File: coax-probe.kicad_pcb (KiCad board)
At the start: 2 copper layers, 28 x 41 mm, 33 parts, among them J1 Conn_01x02, J2 SMA, J3 Conn_01x02, J4 Conn_01x03, J5 SMA, J6 Conn_01x02, U1 OPA690, U2 INA128, U3 OPA690, U4 CJ431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

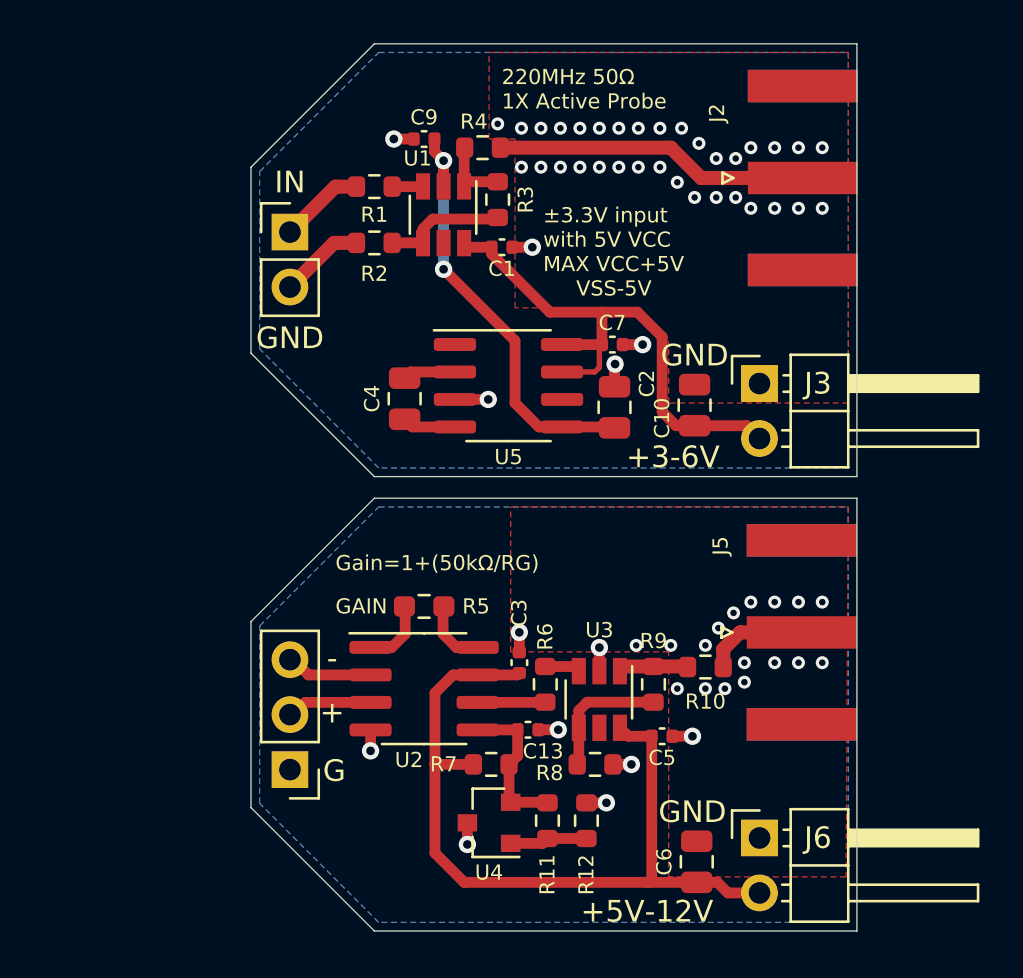
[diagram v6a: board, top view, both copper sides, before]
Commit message: Try out the LMH6642
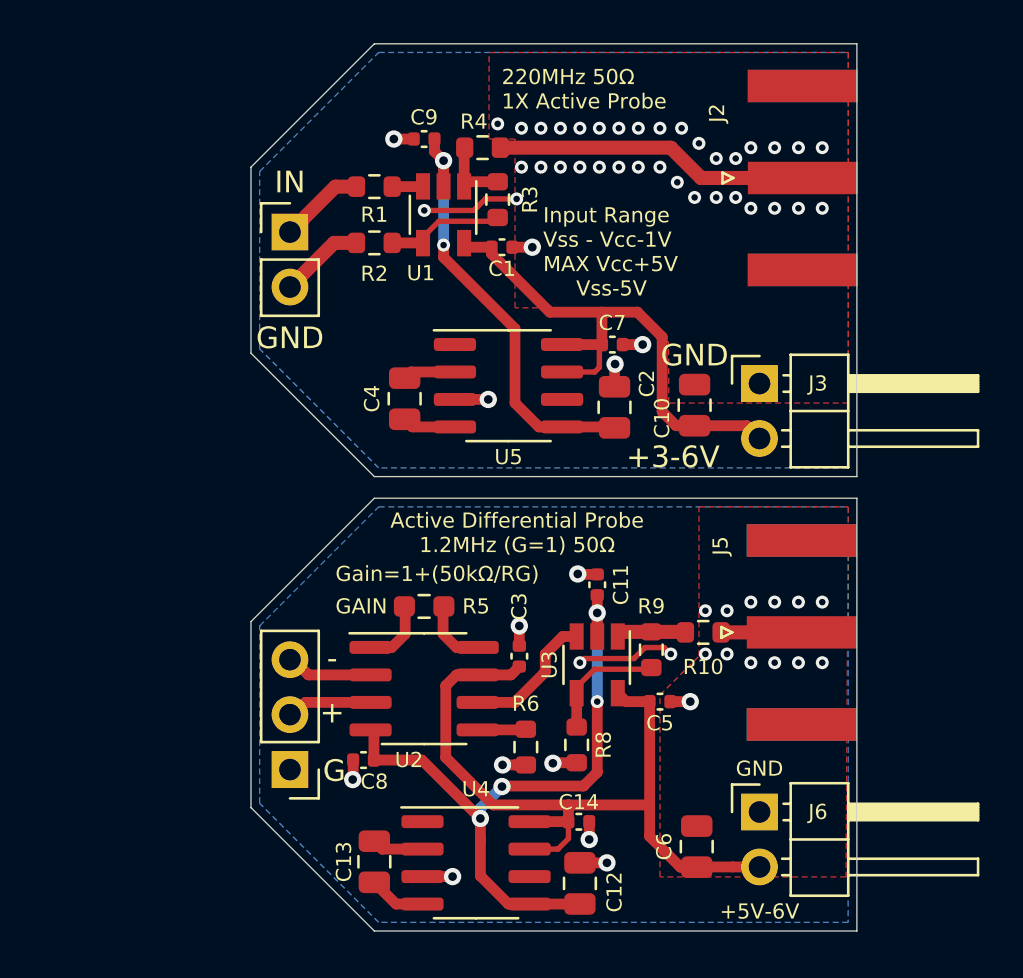
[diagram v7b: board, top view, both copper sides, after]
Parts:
- removed R11: 0, Resistor_SMD:R_0603_1608Metric
- removed R12: DNP, Resistor_SMD:R_0603_1608Metric
- removed R7: 175, Resistor_SMD:R_0603_1608Metric
- added C11: 100nF, Capacitor_SMD:C_0402_1005Metric, F.Cu at (173.0, 75.0)
- added C12: 10uF, Capacitor_SMD:C_0805_2012Metric, F.Cu at (172.2, 88.8)
- added C14: 100nF, Capacitor_SMD:C_0402_1005Metric, F.Cu at (172.2, 86.0)
- added C8: 100nF, Capacitor_SMD:C_0402_1005Metric, F.Cu at (162.2, 83.1)
- C13: value 100nF -> 10uF; footprint Capacitor_SMD:C_0402_1005Metric -> Capacitor_SMD:C_0805_2012Metric
- R1: value 175 -> 510
- R2, R3, R8, R9: value 402 -> 510
- R6: value 175 -> 0
- U1, U3: value OPA690 -> LMH6642; footprint Package_TO_SOT_SMD:TSOT-23-6 -> Package_TO_SOT_SMD:TSOT-23-5
- U4: value CJ431 -> ICL7660; footprint Package_TO_SOT_SMD:SOT-23 -> Package_SO:SOIC-8_3.9x4.9mm_P1.27mm
- moved C13 9.36 mm to (162.7, 87.8), turned to 270 degrees
- moved R6 3.04 mm to (169.7, 82.5)
- moved U4 1.94 mm to (167.4, 87.8), turned to 0 degrees
- moved C5 1.60 mm to (175.9, 80.4)
- moved R10 1.60 mm to (177.9, 77.2)
- moved R9 1.60 mm to (175.5, 78.0)
- moved U3 1.60 mm to (173.0, 78.7)
- moved R8 1.24 mm to (172.1, 82.4), turned to 270 degrees
- moved J6 1.20 mm to (180.5, 85.5)
- moved C6 0.70 mm to (177.6, 87.1)
- moved C3 0.30 mm to (169.4, 78.3)
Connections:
- C13 pad 1: REF -> Net-(C13-Pad1)
- C13 pad 2: GND -> Net-(C13-Pad2)
- R6 pad 1: Net-(R6-Pad1) -> /Vref
- R6 pad 2: /INA -> GND
- U1 pad 5: (no net) -> VCC
- U2 pad 4: GND -> VSS
- U2 pad 5: REF -> /Vref
- U3 pad 2: GND -> VSS
- U3 pad 3: Net-(R6-Pad1) -> /INA
- U3 pad 5: (no net) -> VCC
- U4 pad 1: Net-(R11-Pad2) -> (no net)
- U4 pad 2: REF -> Net-(C13-Pad1)
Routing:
- net VSS: track 20.0 -> 51.1 mm, vias 2 -> 6
- net GND: track 16.9 -> 27.7 mm
- net REF: track 6.70 -> 0.00 mm
- net Net-(R11-Pad2): track 3.44 -> 0.00 mm
- net /INA: track 3.13 -> 6.32 mm
- net Net-(C13-Pad2): track 0.00 -> 2.64 mm
- net Net-(C13-Pad1): track 0.00 -> 2.38 mm
- net /Vref: track 0.00 -> 2.24 mm
- net Net-(R6-Pad1): track 1.64 -> 0.00 mm
- net VCC: track 63.1 -> 61.6 mm
- net /OUTD: track 4.77 -> 3.72 mm
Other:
- board text added: "ICM: -2V − Vcc+2V MAX: ±40V to GND"
- board text added: "Input Range Vss - Vcc-1V MAX Vcc+5V Vss-5V"
- board text removed: "ICM: -2V−VCC+2V MAX: ±40V to GND"
- board text removed: "±3.3V input with 5V VCC MAX VCC+5V VSS-5V"
